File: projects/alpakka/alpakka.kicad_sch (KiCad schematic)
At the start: 56 parts, among them P1 Conn_01x20_Pin, P2 Conn_01x20_Pin, P3 Headers 4P IN, P4 Blade, P5 Jack 2.5mm, P6 Conn_01x02, U1 Alpsalpine_RKJXV, U10 ST_LSM6, U12 ST_LSM6, U2 Alpsalpine_RKJXV, U3 Alpsalpine_EC10E, U6 NXP_PCAL6416A, U8 NXP_PCAL6416A

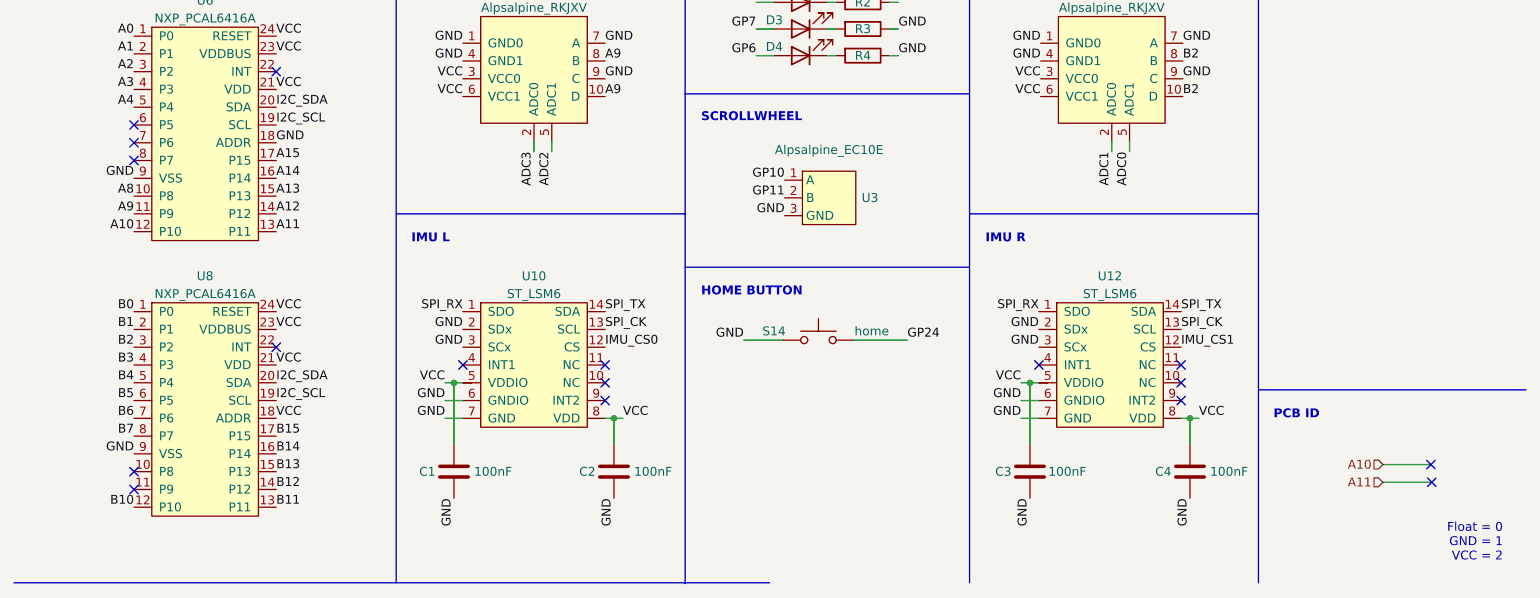
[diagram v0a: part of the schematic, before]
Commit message: Updated hardware generation detection
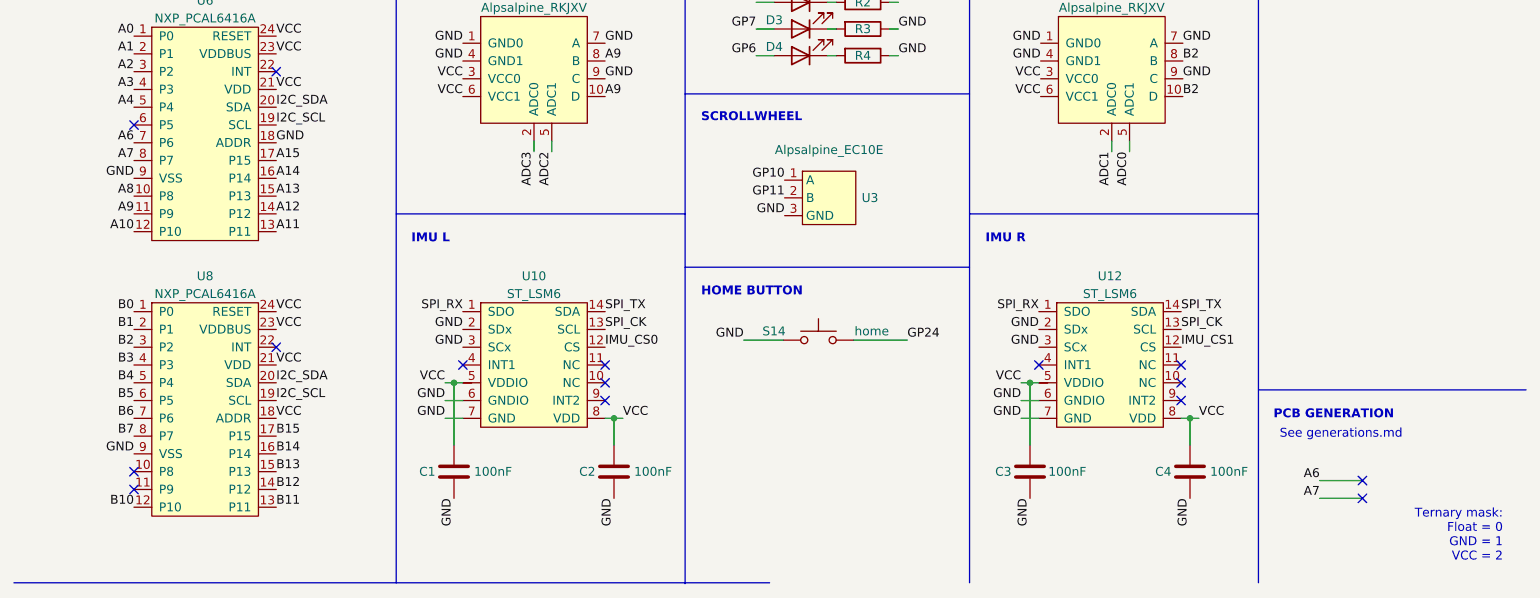
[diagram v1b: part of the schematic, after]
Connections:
- net A6: now reaches U6.7 (P6)
- net A7: now reaches U6.8 (P7)
- no-connect marks 24 -> 22
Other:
- note added: "PCB GENERATION"
- note added: "See generations.md"
- note added: "Ternary mask: Float = 0 GND = 1 VCC = 2"
- note removed: "Float = 0 GND = 1 VCC = 2"
- note removed: "PCB ID"
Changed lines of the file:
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@@
 	)
 	(no_connect
-		(at 214.63 161.544)
+		(at 204.724 163.83)
 	)
 	(no_connect
@@
 	)
 	(no_connect
-		(at 214.503 159.004)
+		(at 204.724 161.29)
 	)
 	(no_connect
@@
 	)
 	(no_connect
-		(at 29.21 113.03)
-	)
-	(no_connect
 		(at 48.26 57.15)
 	)
@@
 	)
 	(no_connect
-		(at 29.21 115.57)
-	)
-	(no_connect
 		(at 178.816 147.32)
 	)
@@
 	(wire
 		(pts
-			(xy 207.645 159.004) (xy 214.503 159.004)
+			(xy 198.628 161.29) (xy 204.724 161.29)
 		)
 		(stroke
@@
 	(wire
 		(pts
-			(xy 207.645 161.544) (xy 214.63 161.544)
+			(xy 198.628 163.83) (xy 204.724 163.83)
 		)
 		(stroke
@@
 		)
 	)
-	(text "PCB ID"
+	(text "PCB GENERATION"
 		(exclude_from_sim no)
 		(at 192.024 152.654 0)
@@
 		)
 	)
-	(text "Float = 0\nGND = 1\nVCC = 2"
+	(text "Ternary mask:\nFloat = 0\nGND = 1\nVCC = 2"
 		(exclude_from_sim no)
-		(at 224.79 170.18 0)
+		(at 224.79 169.164 0)
 		(effects
 			(font
@@
 		)
 	)
+	(text "See generations.md"
+		(exclude_from_sim no)
+		(at 201.676 154.686 0)
+		(effects
+			(font
+				(size 1.27 1.27)
+			)
+		)
+	)
 	(label "A4"
 		(at 29.21 107.95 180)
@@
 		)
 	)
+	(label "A7"
+		(at 198.628 163.83 180)
+		(fields_autoplaced yes)
+		(effects
+			(font
+				(size 1.27 1.27)
+			)
+			(justify right bottom)
+		)
+	)
 	(label "GND"
 		(at 73.66 149.86 180)
@@
 		)
 	)
+	(label "A6"
+		(at 198.628 161.29 180)
+		(fields_autoplaced yes)
+		(effects
+			(font
+				(size 1.27 1.27)
+			)
+			(justify right bottom)
+		)
+	)
 	(label "SPI_CK"
 		(at 48.26 74.93 0)
@@
 		)
 	)
+	(label "A6"
+		(at 29.21 113.03 180)
+		(fields_autoplaced yes)
+		(effects
+			(font
+				(size 1.27 1.27)
+			)
+			(justify right bottom)
+		)
+	)
 	(label "RUN"
 		(at 124.46 29.718 180)
@@
 		)
 	)
+	(label "A7"
+		(at 29.21 115.57 180)
+		(fields_autoplaced yes)
+		(effects
+			(font
+				(size 1.27 1.27)
+			)
+			(justify right bottom)
+		)
+	)
 	(label "GND"
 		(at 208.28 31.75 180)
@@
 		)
 	)
-	(hierarchical_label "A11"
-		(shape input)
-		(at 207.645 161.544 180)
-		(fields_autoplaced yes)
-		(effects
-			(font
-				(size 1.27 1.27)
-			)
-			(justify right)
-		)
-	)
-	(hierarchical_label "A10"
-		(shape input)
-		(at 207.645 159.004 180)
-		(fields_autoplaced yes)
-		(effects
-			(font
-				(size 1.27 1.27)
-			)
-			(justify right)
-		)
-	)

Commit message: Remove DNP resistor from BOM
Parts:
- R7: Export yes -> (none); Mount SMD -> (none)
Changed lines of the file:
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@@
 			)
 		)
-		(property "Mount" "SMD"
+		(property "Mount" ""
 			(at 163.322 74.422 0)
 			(effects
@@
 			)
 		)
-		(property "Export" "yes"
+		(property "Export" ""
 			(at 163.322 74.422 0)
 			(effects

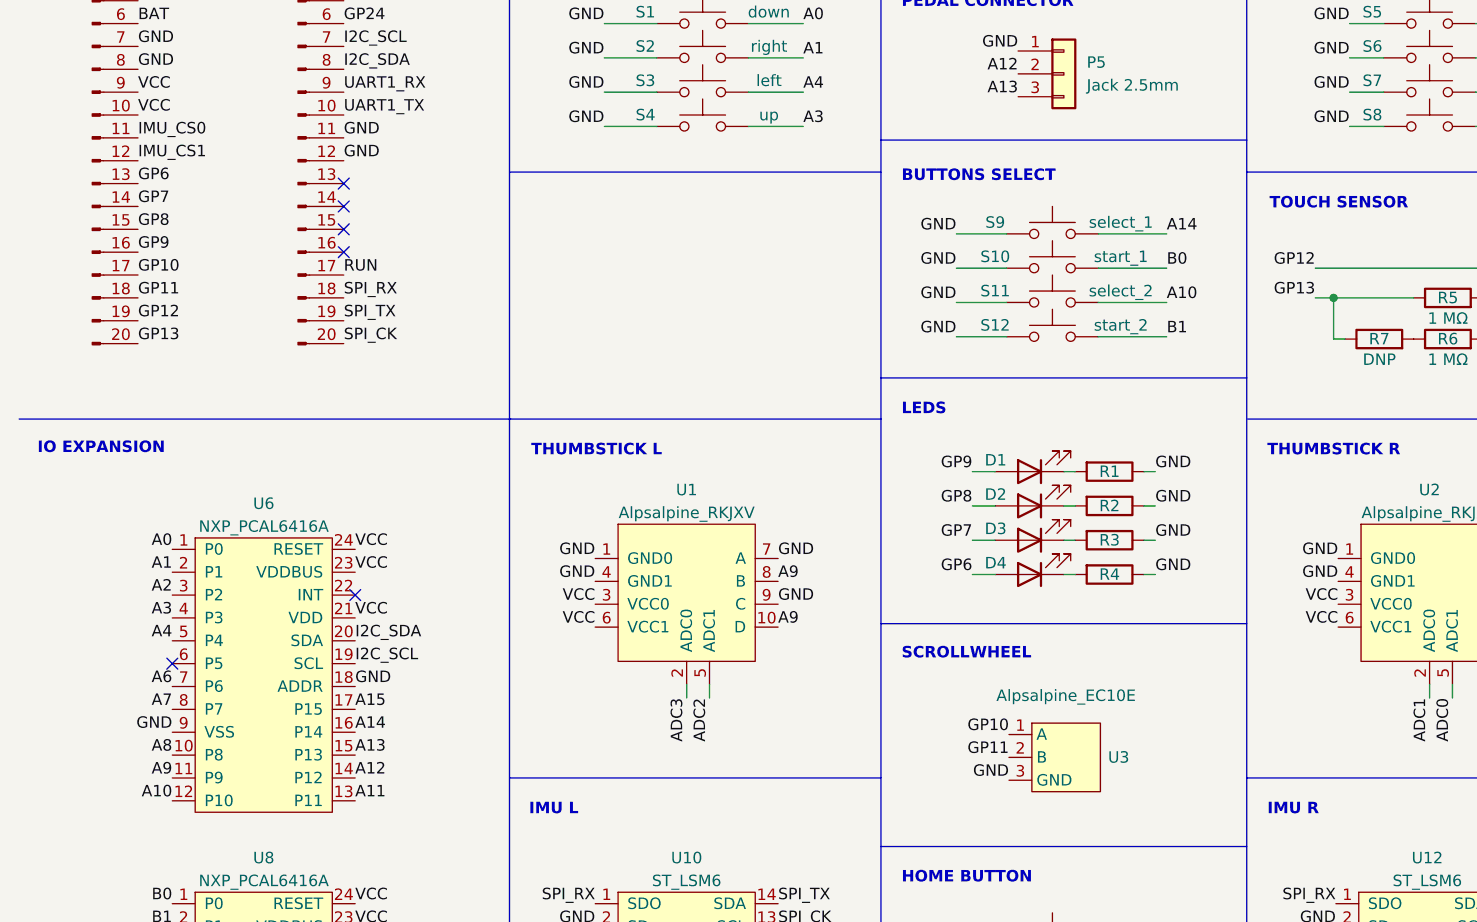
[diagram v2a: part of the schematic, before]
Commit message: Shifted GPIO nets on the bottom row of the top connector
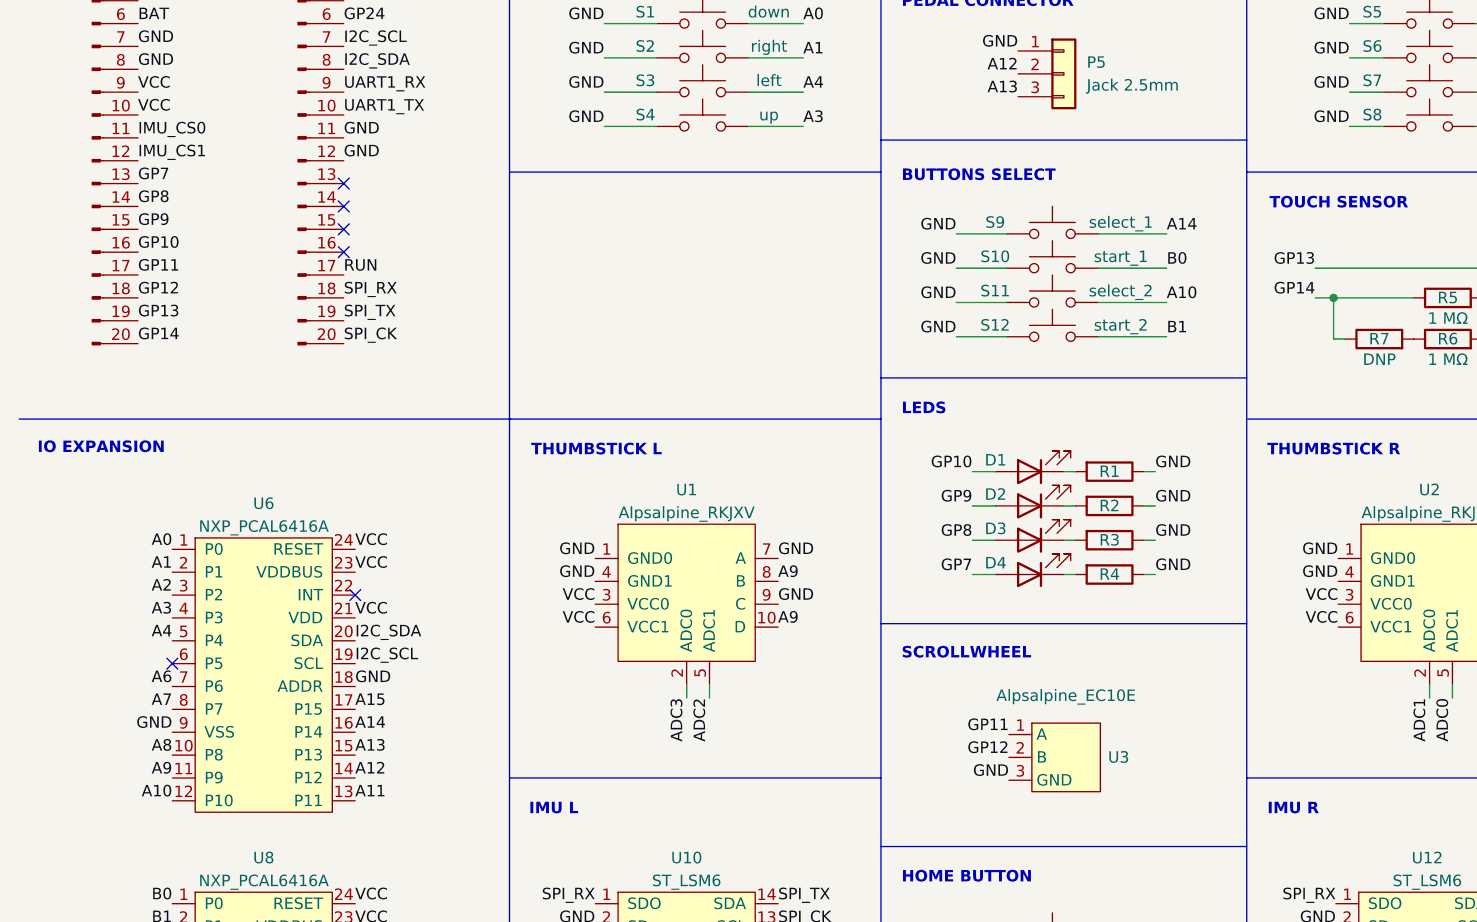
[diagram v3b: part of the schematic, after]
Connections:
- net GP6 is gone; now on net GP7: D4.2 (A), P1.13 (Pin_13)
- net GP10: now also D1.2 (A), P1.16 (Pin_16); no longer P1.17 (Pin_17), U3.1 (A)
- net GP11: now also P1.17 (Pin_17), U3.1 (A); no longer P1.18 (Pin_18), U3.2 (B)
- net GP12: now also P1.18 (Pin_18), U3.2 (B); no longer P1.19 (Pin_19), P4.1, R5.2, R6.2
- net GP13: now also P1.19 (Pin_19), P4.1, R5.2, R6.2; no longer P1.20 (Pin_20), R5.1, R7.1
- net GP7: no longer D3.2 (A), P1.14 (Pin_14)
- net GP8: now also D3.2 (A), P1.14 (Pin_14); no longer D2.2 (A), P1.15 (Pin_15)
- net GP9: now also D2.2 (A), P1.15 (Pin_15); no longer D1.2 (A), P1.16 (Pin_16)
- new net GP14: P1.20 (Pin_20), R5.1, R7.1
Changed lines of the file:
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@@
 		)
 	)
-	(label "GP6"
+	(label "GP7"
 		(at 118.11 100.584 180)
 		(fields_autoplaced yes)
@@
 	)
 	(label "GP9"
-		(at 25.4 64.77 0)
+		(at 25.4 62.23 0)
 		(fields_autoplaced yes)
 		(effects
@@
 	)
 	(label "GP11"
-		(at 25.4 69.85 0)
+		(at 25.4 67.31 0)
 		(fields_autoplaced yes)
 		(effects
@@
 	)
 	(label "GP13"
-		(at 25.4 74.93 0)
+		(at 25.4 72.39 0)
 		(fields_autoplaced yes)
 		(effects
@@
 		)
 	)
-	(label "GP6"
-		(at 25.4 57.15 0)
-		(fields_autoplaced yes)
-		(effects
-			(font
-				(size 1.27 1.27)
-			)
-			(justify left bottom)
-		)
-	)
 	(label "GND"
 		(at 158.75 101.346 180)
@@
 		)
 	)
-	(label "GP11"
+	(label "GP12"
 		(at 122.174 120.904 180)
 		(fields_autoplaced yes)
@@
 	)
 	(label "GP8"
-		(at 25.4 62.23 0)
-		(fields_autoplaced yes)
-		(effects
-			(font
-				(size 1.27 1.27)
-			)
-			(justify left bottom)
-		)
-	)
-	(label "GP9"
+		(at 25.4 59.69 0)
+		(fields_autoplaced yes)
+		(effects
+			(font
+				(size 1.27 1.27)
+			)
+			(justify left bottom)
+		)
+	)
+	(label "GP10"
 		(at 118.11 89.154 180)
 		(fields_autoplaced yes)
@@
 		)
 	)
-	(label "GP12"
+	(label "GP13"
 		(at 156.21 66.548 180)
 		(fields_autoplaced yes)
@@
 	)
 	(label "GP12"
-		(at 25.4 72.39 0)
+		(at 25.4 69.85 0)
 		(fields_autoplaced yes)
 		(effects
@@
 		)
 	)
-	(label "GP13"
+	(label "GP14"
 		(at 156.21 69.85 180)
 		(fields_autoplaced yes)
@@
 		)
 	)
-	(label "GP7"
+	(label "GP8"
 		(at 118.11 96.774 180)
 		(fields_autoplaced yes)
@@
 	)
 	(label "GP7"
-		(at 25.4 59.69 0)
+		(at 25.4 57.15 0)
 		(fields_autoplaced yes)
 		(effects
@@
 	)
 	(label "GP10"
-		(at 25.4 67.31 0)
+		(at 25.4 64.77 0)
 		(fields_autoplaced yes)
 		(effects
@@
 		)
 	)
+	(label "GP14"
+		(at 25.4 74.93 0)
+		(fields_autoplaced yes)
+		(effects
+			(font
+				(size 1.27 1.27)
+			)
+			(justify left bottom)
+		)
+	)
 	(label "GND"
 		(at 77.216 46.99 180)
@@
 		)
 	)
-	(label "GP8"
+	(label "GP9"
 		(at 118.11 92.964 180)
 		(fields_autoplaced yes)
@@
 		)
 	)
-	(label "GP10"
+	(label "GP11"
 		(at 122.174 118.364 180)
 		(fields_autoplaced yes)
